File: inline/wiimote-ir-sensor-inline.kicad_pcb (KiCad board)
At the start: 2 copper layers, 13 x 16 mm, 10 parts, among them J1 Conn_01x04_Pin, U2 AP2112-3.3V, X1 SG3225CAN 24.0000M-TJGA3

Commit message: Fix BOM and schematic R3 value
(Thanks to RetroMidget for spotting this!)
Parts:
- R3: value 330K -> 33K
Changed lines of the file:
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@@
 	(net 9 "unconnected-(U2-NC-Pad4)")
 	(net 10 "unconnected-(X1-~{ST}-Pad1)")
+	(net 11 "unconnected-(U1-NC-Pad4)_0")
 	(footprint "Resistor_SMD:R_0603_1608Metric_Pad0.98x0.95mm_HandSolder"
 		(layer "F.Cu")
@@
 			)
 		)
-		(property "Value" "330K"
+		(property "Value" "33K"
 			(at 0 1.43 90)
 			(layer "F.Fab")
@@
 			)
 		)
-		(property "Footprint" ""
+		(property "Footprint" "Resistor_SMD:R_0603_1608Metric_Pad0.98x0.95mm_HandSolder"
 			(at 0 0 90)
 			(unlocked yes)
@@
 			)
 		)
-		(property "Description" "Resistor"
+		(property "Description" ""
 			(at 0 0 90)
 			(unlocked yes)
@@
 			)
 		)
+		(property ki_fp_filters "R_*")
+		(sheetname "Root")
+		(sheetfile "wiimote-ir-sensor-inline.kicad_sch")
 		(attr smd)
 		(fp_line
@@
 			)
 		)
-		(property "Footprint" ""
+		(property "Footprint" "Connector_PinHeader_2.54mm:PinHeader_1x04_P2.54mm_Vertical"
 			(at 0 0 -90)
 			(unlocked yes)
@@
 			)
 		)
-		(property "Description" "Generic connector, single row, 01x04, script generated"
+		(property "Description" ""
 			(at 0 0 -90)
 			(unlocked yes)
@@
 			)
 		)
+		(property ki_fp_filters "Connector*:*_1x??_*")
+		(sheetname "Root")
+		(sheetfile "wiimote-ir-sensor-inline.kicad_sch")
 		(attr through_hole)
 		(fp_line
@@
 			)
 		)
-		(property "Footprint" ""
+		(property "Footprint" "Resistor_SMD:R_0603_1608Metric_Pad0.98x0.95mm_HandSolder"
 			(at 0 0 90)
 			(unlocked yes)
@@
 			)
 		)
-		(property "Description" "Resistor"
+		(property "Description" ""
 			(at 0 0 90)
 			(unlocked yes)
@@
 			)
 		)
+		(property ki_fp_filters "R_*")
+		(sheetname "Root")
+		(sheetfile "wiimote-ir-sensor-inline.kicad_sch")
 		(attr smd)
 		(fp_line
@@
 			)
 		)
-		(property "Footprint" ""
+		(property "Footprint" "Resistor_SMD:R_0603_1608Metric_Pad0.98x0.95mm_HandSolder"
 			(at 0 0 -90)
 			(unlocked yes)
@@
 			)
 		)
-		(property "Description" "Resistor"
+		(property "Description" ""
 			(at 0 0 -90)
 			(unlocked yes)
@@
 			)
 		)
+		(property ki_fp_filters "R_*")
+		(sheetname "Root")
+		(sheetfile "wiimote-ir-sensor-inline.kicad_sch")
 		(attr smd)
 		(fp_line
@@
 			)
 		)
-		(property "Footprint" ""
+		(property "Footprint" "Package_TO_SOT_SMD:SOT-23-5"
 			(at 0 0 90)
 			(unlocked yes)
@@
 			)
 		)
-		(property "Datasheet" ""
+		(property "Datasheet" "https://www.diodes.com/assets/Datasheets/AP2112.pdf"
 			(at 0 0 90)
 			(unlocked yes)
@@
 			)
 		)
-		(property "Description" "600mA low dropout linear regulator, with enable pin, 3.8V-6V input voltage range, 3.3V fixed positive output, SOT-23-5"
+		(property "Description" ""
 			(at 0 0 90)
 			(unlocked yes)
@@
 			)
 		)
+		(property ki_fp_filters "SOT?23?5*")
+		(sheetname "Root")
+		(sheetfile "wiimote-ir-sensor-inline.kicad_sch")
 		(attr smd)
 		(fp_line
@@
 			)
 		)
-		(property "Footprint" ""
+		(property "Footprint" "Oscillator:Oscillator_SMD_SeikoEpson_SG8002CE-4Pin_3.2x2.5mm_HandSoldering"
 			(at 0 0 180)
 			(unlocked yes)
@@
 			)
 		)
-		(property "Datasheet" ""
+		(property "Datasheet" "https://support.epson.biz/td/api/doc_check.php?dl=brief_SG5032CAN&lang=en"
 			(at 0 0 180)
 			(unlocked yes)
@@
 			)
 		)
-		(property "Description" "CMOS Clock Oscillator 1 to 75 MHz"
+		(property "Description" ""
 			(at 0 0 180)
 			(unlocked yes)
@@
 			)
 		)
+		(property ki_fp_filters "Oscillator*SMD*SeikoEpson*SG8002LB*5.0x3.2mm*")
+		(sheetname "Root")
+		(sheetfile "wiimote-ir-sensor-inline.kicad_sch")
 		(attr smd)
 		(fp_circle
@@
 			)
 		)
-		(property "Footprint" ""
+		(property "Footprint" "Capacitor_SMD:C_0603_1608Metric_Pad1.08x0.95mm_HandSolder"
 			(at 0 0 0)
 			(unlocked yes)
@@
 			)
 		)
-		(property "Description" "Unpolarized capacitor"
+		(property "Description" ""
 			(at 0 0 0)
 			(unlocked yes)
@@
 			)
 		)
+		(property ki_fp_filters "C_*")
+		(sheetname "Root")
+		(sheetfile "wiimote-ir-sensor-inline.kicad_sch")
 		(attr smd)
 		(fp_line
@@
 			)
 		)
-		(property "Footprint" ""
+		(property "Footprint" "Capacitor_SMD:C_0603_1608Metric_Pad1.08x0.95mm_HandSolder"
 			(at 0 0 0)
 			(unlocked yes)
@@
 			)
 		)
-		(property "Description" "Unpolarized capacitor"
+		(property "Description" ""
 			(at 0 0 0)
 			(unlocked yes)
@@
 			)
 		)
+		(property ki_fp_filters "C_*")
+		(sheetname "Root")
+		(sheetfile "wiimote-ir-sensor-inline.kicad_sch")
 		(attr smd)
 		(fp_line
@@
 			)
 		)
-		(property "Footprint" ""
+		(property "Footprint" "GUN4IR:wiimote-pixart-camera-inline"
 			(at 0 0 180)
 			(unlocked yes)
@@
 			)
 		)
+		(sheetname "Root")
+		(sheetfile "wiimote-ir-sensor-inline.kicad_sch")
 		(attr through_hole)
 		(fp_line
@@
 			(size 0.6 3.5)
 			(layers "B.Cu" "B.Mask")
-			(net 7 "unconnected-(U1-NC-Pad4)")
+			(net 11 "unconnected-(U1-NC-Pad4)_0")
 			(pinfunction "NC")
 			(pintype "no_connect")
@@
 			)
 		)
-		(property "Footprint" ""
+		(property "Footprint" "Capacitor_SMD:C_0603_1608Metric_Pad1.08x0.95mm_HandSolder"
 			(at 0 0 0)
 			(unlocked yes)
@@
 			)
 		)
-		(property "Description" "Unpolarized capacitor"
+		(property "Description" ""
 			(at 0 0 0)
 			(unlocked yes)
@@
 			)
 		)
+		(property ki_fp_filters "C_*")
+		(sheetname "Root")
+		(sheetfile "wiimote-ir-sensor-inline.kicad_sch")
 		(attr smd)
 		(fp_line

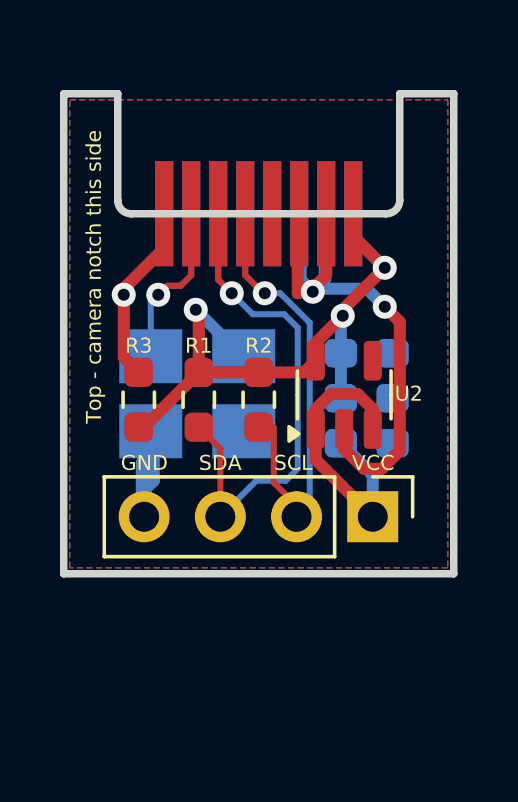
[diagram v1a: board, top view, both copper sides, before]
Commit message: Instate superslim variant as new inline
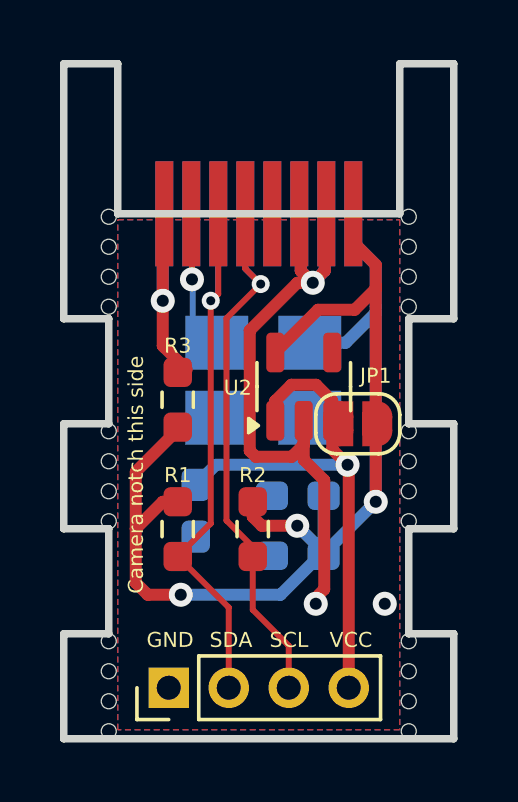
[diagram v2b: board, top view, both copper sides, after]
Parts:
- added JP1: SolderJumper_2_Open, Jumper:SolderJumper-2_P1.3mm_Open_RoundedPad1.0x1.5mm, F.Cu at (109.8, 111.0)
- added REF**: NPTH-0.5mm, Panelization:NPTH-0.5mm, F.Cu at (111.5, 119.2)
- added REF**: NPTH-0.5mm, Panelization:NPTH-0.5mm, F.Cu at (101.5, 107.1)
- added REF**: NPTH-0.5mm, Panelization:NPTH-0.5mm, F.Cu at (101.5, 114.2)
- added REF**: NPTH-0.5mm, Panelization:NPTH-0.5mm, F.Cu at (111.5, 118.2)
- added REF**: NPTH-0.5mm, Panelization:NPTH-0.5mm, F.Cu at (101.5, 120.2)
- added REF**: NPTH-0.5mm, Panelization:NPTH-0.5mm, F.Cu at (111.5, 104.1)
- added REF**: NPTH-0.5mm, Panelization:NPTH-0.5mm, F.Cu at (101.5, 111.2)
- added REF**: NPTH-0.5mm, Panelization:NPTH-0.5mm, F.Cu at (111.5, 114.2)
- added REF**: NPTH-0.5mm, Panelization:NPTH-0.5mm, F.Cu at (101.5, 105.1)
- added REF**: NPTH-0.5mm, Panelization:NPTH-0.5mm, F.Cu at (111.5, 111.2)
- added REF**: NPTH-0.5mm, Panelization:NPTH-0.5mm, F.Cu at (101.5, 118.2)
- added REF**: NPTH-0.5mm, Panelization:NPTH-0.5mm, F.Cu at (111.5, 121.2)
- added REF**: NPTH-0.5mm, Panelization:NPTH-0.5mm, F.Cu at (111.5, 113.2)
- added REF**: NPTH-0.5mm, Panelization:NPTH-0.5mm, F.Cu at (111.5, 120.2)
- added REF**: NPTH-0.5mm, Panelization:NPTH-0.5mm, F.Cu at (101.5, 113.2)
- added REF**: NPTH-0.5mm, Panelization:NPTH-0.5mm, F.Cu at (111.5, 106.1)
- added REF**: Tab, PCM_kikit:Tab, F.Cu at (112.1, 99.0)
- added REF**: NPTH-0.5mm, Panelization:NPTH-0.5mm, F.Cu at (101.5, 119.2)
- added REF**: NPTH-0.5mm, Panelization:NPTH-0.5mm, F.Cu at (111.5, 112.2)
- added REF**: NPTH-0.5mm, Panelization:NPTH-0.5mm, F.Cu at (101.5, 104.1)
- added REF**: NPTH-0.5mm, Panelization:NPTH-0.5mm, F.Cu at (111.5, 105.1)
- added REF**: NPTH-0.5mm, Panelization:NPTH-0.5mm, F.Cu at (111.5, 107.1)
- added REF**: NPTH-0.5mm, Panelization:NPTH-0.5mm, F.Cu at (101.5, 121.2)
- added REF**: NPTH-0.5mm, Panelization:NPTH-0.5mm, F.Cu at (101.5, 106.1)
- added REF**: NPTH-0.5mm, Panelization:NPTH-0.5mm, F.Cu at (101.5, 112.2)
- J1: footprint Connector_PinHeader_2.54mm:PinHeader_1x04_P2.54mm_Vertical -> Connector_PinHeader_2.00mm:PinHeader_1x04_P2.00mm_Vertical
- U1: footprint GUN4IR:wiimote-pixart-camera-inline -> GUN4IR:wiimote-pixart-camera-inline_slim
- moved J1 8.87 mm to (103.5, 119.8), turned to 90 degrees
- moved C1 7.13 mm to (107.8, 115.4), turned to 180 degrees
- moved C3 6.13 mm to (104.4, 113.9), turned to -90 degrees
- moved R1 4.37 mm to (103.8, 114.5)
- moved R2 4.32 mm to (106.3, 114.5)
- moved C2 3.98 mm to (107.8, 113.4), turned to 180 degrees
- moved X1 2.25 mm to (106.7, 109.5)
- moved U2 1.38 mm to (108.0, 109.8)
- moved R3 1.30 mm to (103.8, 110.2)
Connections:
- C3 pad 1: +5V -> VCC
- J1 pad 1: +5V -> GND
- J1 pad 2: /SCL -> /SDA
- J1 pad 3: /SDA -> /SCL
- J1 pad 4: GND -> VCC
- U2 pad 1: +5V -> VCC
- U2 pad 3: +5V -> VCC
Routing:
- net +3.3V: track 22.6 -> 46.7 mm
- net VCC: track 0.00 -> 18.1 mm, vias 0 -> 1
- net +5V: track 10.1 -> 0.00 mm
- net GND: track 24.9 -> 19.6 mm, vias 2 -> 3
- net /CLK: track 8.79 -> 5.07 mm
- net /SDA: track 19.6 -> 18.7 mm
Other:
- board size 13 x 16 mm -> 13 x 22.5 mm
- board text added: "Camera notch this side"
- board text removed: "Top - camera notch this side"

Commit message: Update inline board to allow wiring clock signal directly
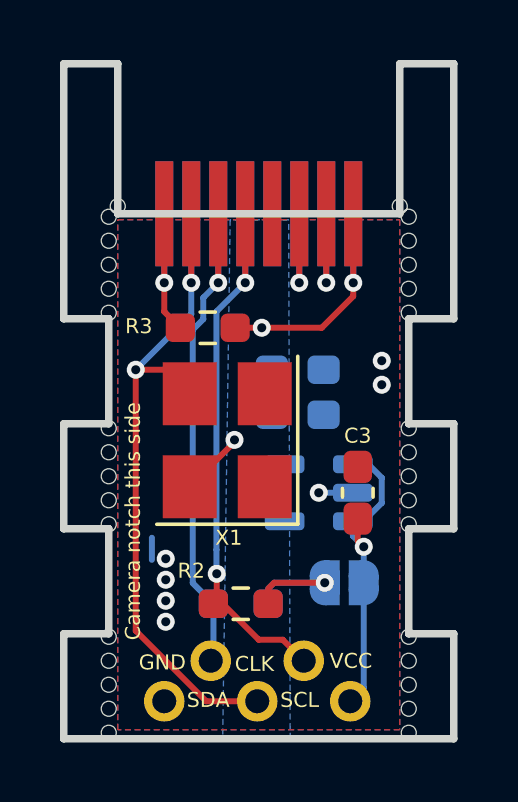
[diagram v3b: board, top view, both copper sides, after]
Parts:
- removed the REF** at (111.5, 119.2)
- removed the REF** at (101.5, 114.2)
- removed the REF** at (111.5, 118.2)
- removed the REF** at (101.5, 120.2)
- removed the REF** at (101.5, 111.2)
- removed the REF** at (111.5, 114.2)
- removed the REF** at (111.5, 111.2)
- removed the REF** at (101.5, 118.2)
- removed the REF** at (111.5, 121.2)
- removed the REF** at (111.5, 113.2)
- removed the REF** at (111.5, 120.2)
- removed the REF** at (101.5, 113.2)
- removed the REF** at (111.5, 106.1)
- removed the REF** at (101.5, 119.2)
- removed the REF** at (111.5, 112.2)
- removed the REF** at (111.5, 105.1)
- removed the REF** at (111.5, 107.1)
- removed the REF** at (101.5, 121.2)
- removed the REF** at (101.5, 112.2)
- added REF**: NPTH-0.5mm, Panelization:NPTH-0.5mm, F.Cu at (111.5, 112.8)
- added REF**: NPTH-0.5mm, Panelization:NPTH-0.5mm, F.Cu at (111.5, 114.3)
- added REF**: NPTH-0.5mm, Panelization:NPTH-0.5mm, F.Cu at (111.2, 103.8)
- added REF**: NPTH-0.5mm, Panelization:NPTH-0.5mm, F.Cu at (101.5, 112.8)
- added REF**: NPTH-0.5mm, Panelization:NPTH-0.5mm, F.Cu at (101.5, 121.3)
- added REF**: NPTH-0.5mm, Panelization:NPTH-0.5mm, F.Cu at (101.5, 120.5)
- added REF**: NPTH-0.5mm, Panelization:NPTH-0.5mm, F.Cu at (111.5, 119.7)
- added REF**: NPTH-0.5mm, Panelization:NPTH-0.5mm, F.Cu at (101.5, 119.7)
- added REF**: NPTH-0.5mm, Panelization:NPTH-0.5mm, F.Cu at (111.5, 118.9)
- added REF**: NPTH-0.5mm, Panelization:NPTH-0.5mm, F.Cu at (101.5, 118.9)
- added REF**: NPTH-0.5mm, Panelization:NPTH-0.5mm, F.Cu at (101.5, 112.0)
- added REF**: NPTH-0.5mm, Panelization:NPTH-0.5mm, F.Cu at (101.5, 114.3)
- added REF**: NPTH-0.5mm, Panelization:NPTH-0.5mm, F.Cu at (111.5, 111.2)
- added REF**: NPTH-0.5mm, Panelization:NPTH-0.5mm, F.Cu at (111.5, 105.7)
- added REF**: NPTH-0.5mm, Panelization:NPTH-0.5mm, F.Cu at (111.5, 106.5)
- added REF**: NPTH-0.5mm, Panelization:NPTH-0.5mm, F.Cu at (111.5, 112.0)
- added REF**: NPTH-0.5mm, Panelization:NPTH-0.5mm, F.Cu at (101.5, 113.5)
- added REF**: NPTH-0.5mm, Panelization:NPTH-0.5mm, F.Cu at (111.5, 118.1)
- added REF**: NPTH-0.5mm, Panelization:NPTH-0.5mm, F.Cu at (111.5, 104.9)
- added REF**: NPTH-0.5mm, Panelization:NPTH-0.5mm, F.Cu at (101.5, 111.2)
- added REF**: NPTH-0.5mm, Panelization:NPTH-0.5mm, F.Cu at (101.8, 103.8)
- added REF**: NPTH-0.5mm, Panelization:NPTH-0.5mm, F.Cu at (111.5, 113.5)
- added REF**: NPTH-0.5mm, Panelization:NPTH-0.5mm, F.Cu at (111.5, 107.3)
- added REF**: NPTH-0.5mm, Panelization:NPTH-0.5mm, F.Cu at (101.5, 107.3)
- added REF**: NPTH-0.5mm, Panelization:NPTH-0.5mm, F.Cu at (111.5, 120.5)
- added REF**: NPTH-0.5mm, Panelization:NPTH-0.5mm, F.Cu at (101.5, 118.1)
- added REF**: NPTH-0.5mm, Panelization:NPTH-0.5mm, F.Cu at (111.5, 121.3)
- C3, X1: moved to F.Cu
- J1: value Conn_01x04_Pin -> Conn_01x05_Pin; footprint Connector_PinHeader_2.00mm:PinHeader_1x04_P2.00mm_Vertical -> wiimote-ir-sensor:5Wires-staggered
- JP1, R1, U2: moved to B.Cu
- U1: footprint GUN4IR:wiimote-pixart-camera-inline_slim -> wiimote-ir-sensor:wiimote-pixart-camera-inline_slim
- moved C1 6.20 mm to (107.8, 109.2), turned to 0 degrees
- moved C3 5.43 mm to (109.8, 113.3), turned to 90 degrees
- moved JP1 5.32 mm to (109.3, 116.3), turned to 180 degrees
- moved U2 3.57 mm to (108.5, 113.3), turned to 180 degrees
- moved R1 3.26 mm to (105.9, 117.0), turned to 180 degrees
- moved J1 2.96 mm to (106.5, 119.6), turned to 0 degrees
- moved C2 2.70 mm to (107.8, 110.7), turned to 0 degrees
- moved R3 2.60 mm to (104.8, 107.8), turned to 180 degrees
- moved R2 2.52 mm to (105.9, 117.0), turned to 0 degrees
- moved X1 2.33 mm to (105.5, 111.5), turned to 90 degrees
- moved REF** 0.60 mm to (101.5, 106.5)
- moved REF** 0.40 mm to (101.5, 105.7)
- moved REF** 0.20 mm to (101.5, 104.9)
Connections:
- J1 pad 3: /SCL -> /CLK
- J1 pad 4: VCC -> /SCL
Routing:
- net +3.3V: track 46.7 -> 15.5 mm, vias 3 -> 4
- net /CLK: track 5.07 -> 24.1 mm, vias 1 -> 2
- net GND: track 19.6 -> 11.1 mm, vias 3 -> 9
- net VCC: track 18.1 -> 10.6 mm
- net /SCL: track 18.6 -> 19.5 mm, vias 1 -> 2
- net Net-(U1-RESET): track 7.23 -> 6.32 mm
- net /SDA: track 18.7 -> 17.9 mm
- added copper zone on B.Cu, net +3.3V
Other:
- board text added: "CLK"
